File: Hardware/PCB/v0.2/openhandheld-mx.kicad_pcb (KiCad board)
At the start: 4 copper layers, 84 x 42 mm, 112 parts, among them J1 TYPE-C-31-M-12, J2 SJ-3524-SMT-TR, J3 Battery, J4 1040310811, J5 PPPC062LFBN-RC, Q1 SI2102-TP, Q2 SI2102-TP, Q3 SI2102-TP, Q4 SI2101-TP, Q5 SI2102-TP, SW1 RESET, SW2 ON/OFF, SW3 A, SW4 B, SW5 START, SW6 SELECT, U1 TLV9061IDCKR, U10 LIS2DE12TR, U11 TLV74333PDBVR, U2 CP2102N-A02-GQFN24, U3 MCP73831T-2ACI_OT, U4 PAM8301AAF, U5 DSC6001CI1A-008.0000T, U6 VSOP38338, U7 AP9211S-AN-HAC-7, U8 STM32L431CCU6, U9 W25Q64JVZPIQ

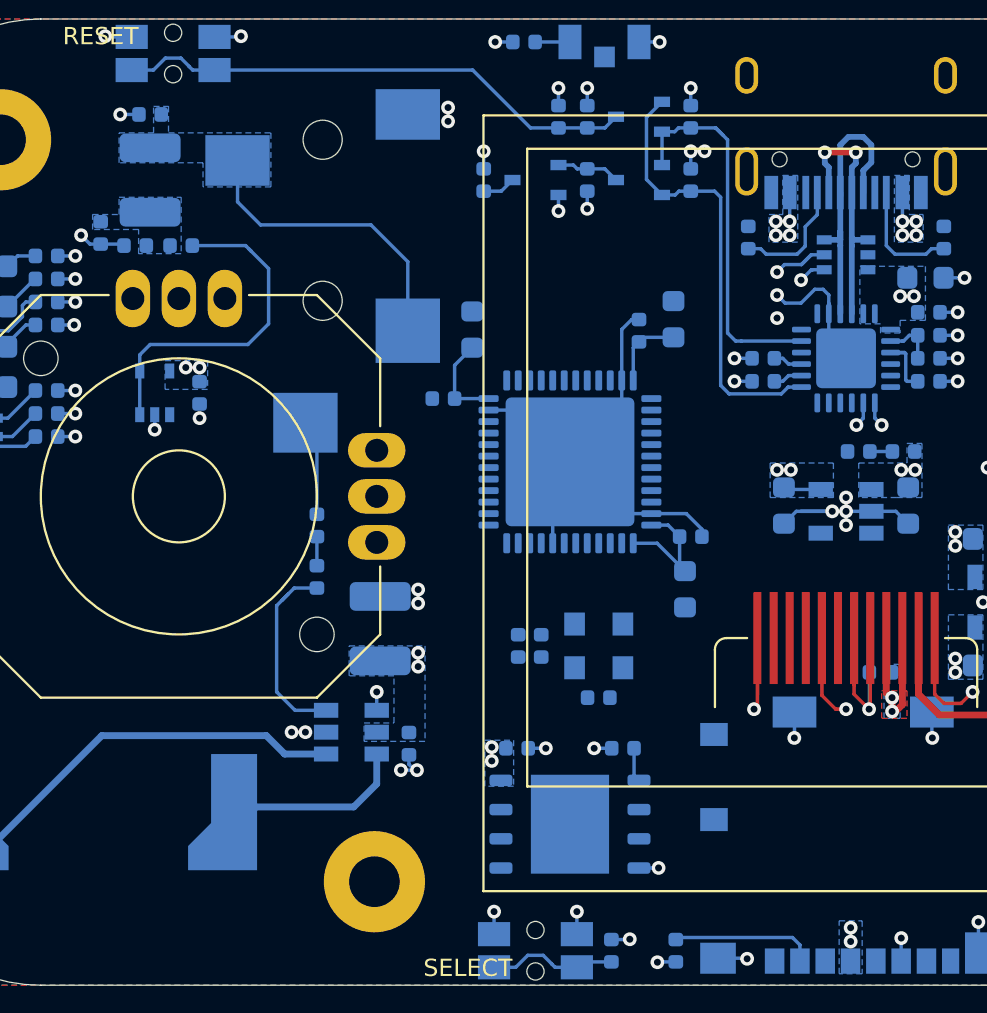
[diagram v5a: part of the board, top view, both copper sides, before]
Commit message: PCB v0.2: STM32 fanout
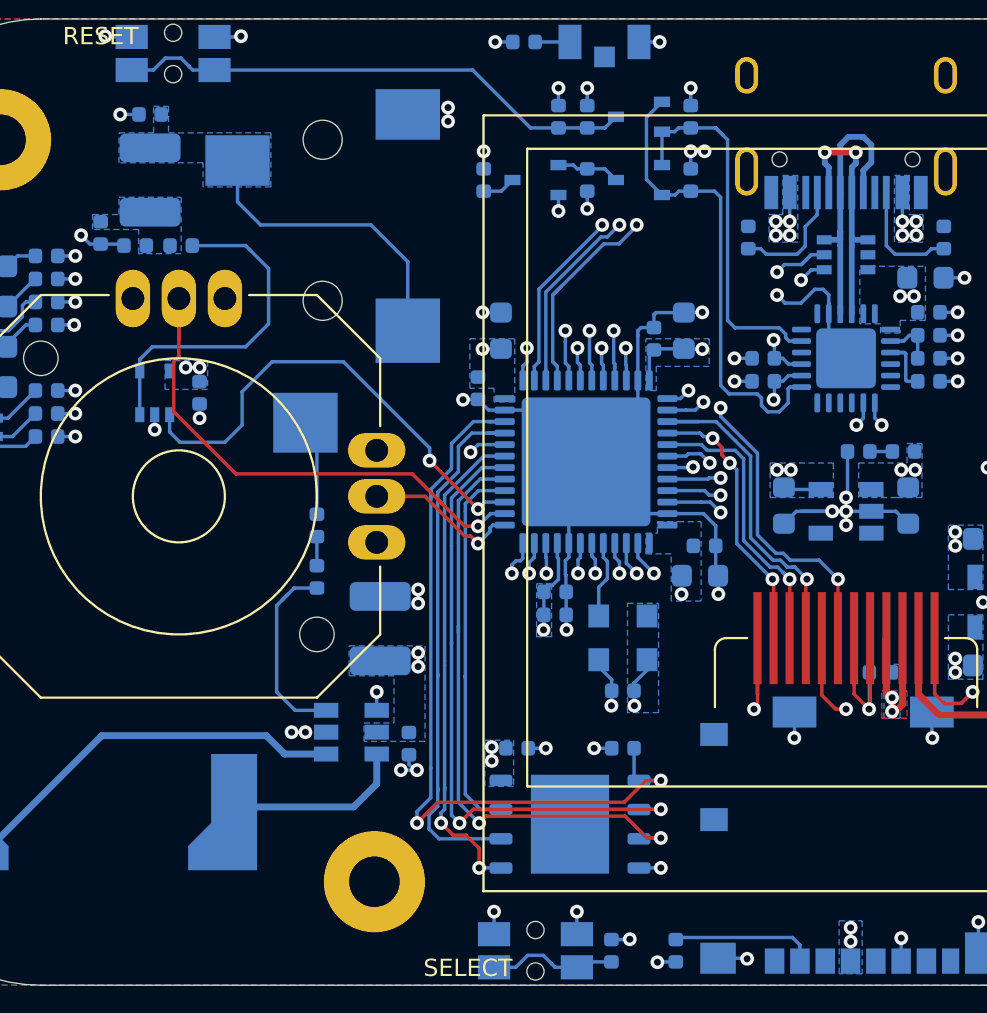
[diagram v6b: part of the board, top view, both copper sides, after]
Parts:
- moved C12 2.43 mm to (-12.7, 3.90), turned to 0 degrees
- moved C10 2.09 mm to (-12.7, 4.90), turned to 0 degrees
- moved C15 1.57 mm to (-16.0, -4.95), turned to 270 degrees
- moved C13 1.25 mm to (-15.0, -7.45)
- moved U5 1.11 mm to (-9.70, 5.90)
- moved C11 1.09 mm to (-9.70, 8.20)
- moved C20 0.88 mm to (-6.35, 3.20), turned to 0 degrees
- moved C19 0.74 mm to (-8.35, -7.10)
- moved C21 0.72 mm to (-6.15, 1.90)
- moved U8 0.70 mm to (-11.3, -1.75)
- moved C17 0.67 mm to (-7.05, -7.45)
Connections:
- D2 pad 2: /LED_RX -> /LED_RXD
- D3 pad 2: /LED_TX -> /LED_TXD
- R11 pad 2: /LED_RX -> /LED_RXD
- R13 pad 2: /LED_TX -> /LED_TXD
- U8 pad 13: /JOY_X -> /JOY_Y
- U8 pad 14: /JOY_Y -> /JOY_X
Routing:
- net /QSPI_NCS: track 1.48 -> 34.7 mm, vias 0 -> 2
- net /QSPI_IO1: track 0.00 -> 27.2 mm, vias 0 -> 2
- net /QSPI_IO2: track 0.00 -> 26.5 mm, vias 0 -> 2
- net /JOY_X: track 0.00 -> 24.2 mm, vias 0 -> 1
- net /QSPI_CLK: track 0.00 -> 23.7 mm
- net /QSPI_IO0: track 0.00 -> 21.7 mm, vias 0 -> 2
- net /DAC_PWM_OUT: track 0.00 -> 20.9 mm, vias 0 -> 2
- net /QSPI_IO3: track 0.00 -> 16.5 mm
- net GND: track 106.2 -> 122.4 mm, vias 59 -> 64
- net /LCD_DC: track 0.00 -> 15.2 mm, vias 0 -> 3
- net /LCD_SCK: track 0.00 -> 15.0 mm, vias 0 -> 1
- net /LCD_MOSI: track 0.00 -> 12.8 mm, vias 0 -> 1
- net /LCD_RESET: track 0.00 -> 11.8 mm, vias 0 -> 3
- net /SPI2_MOSI: track 0.00 -> 9.48 mm, vias 0 -> 1
- net /SPI2_MISO: track 0.00 -> 8.69 mm, vias 0 -> 1
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
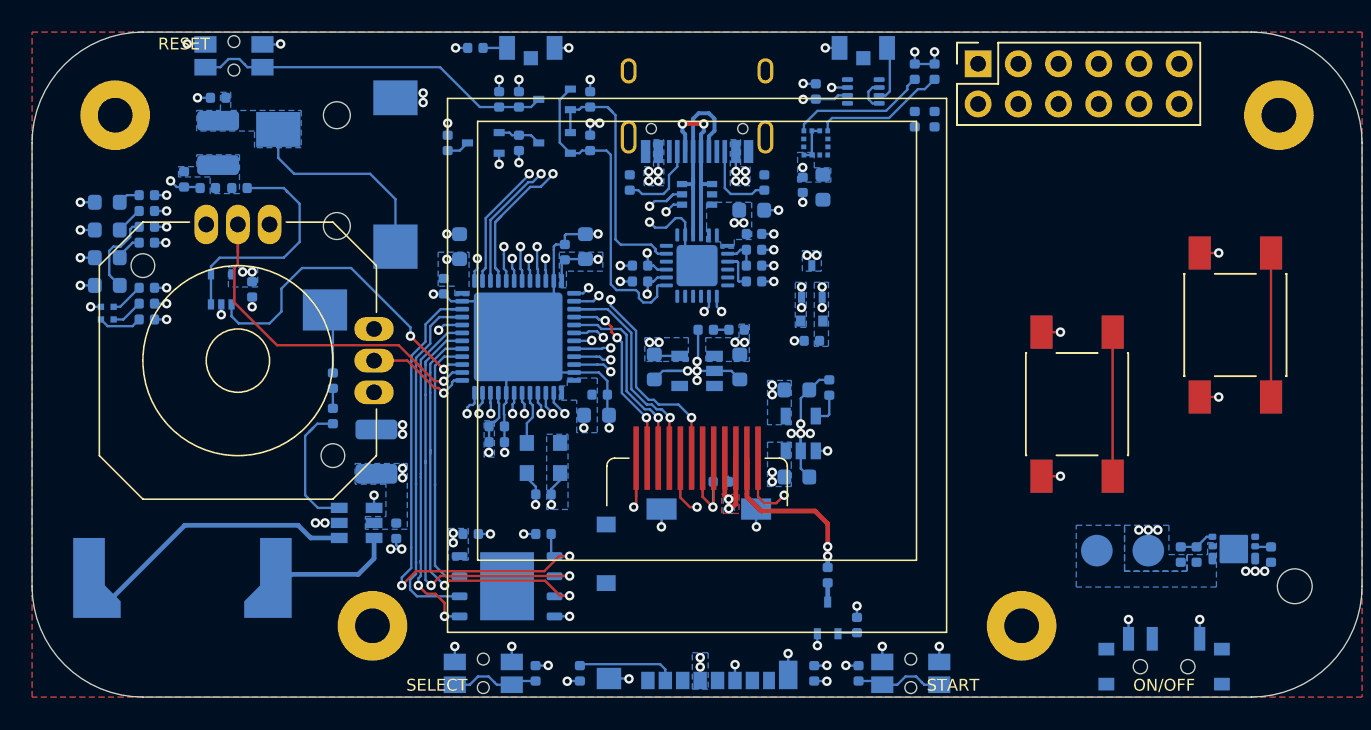
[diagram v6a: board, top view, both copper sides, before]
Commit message: PCB v0.2: Finished placement. Routing...
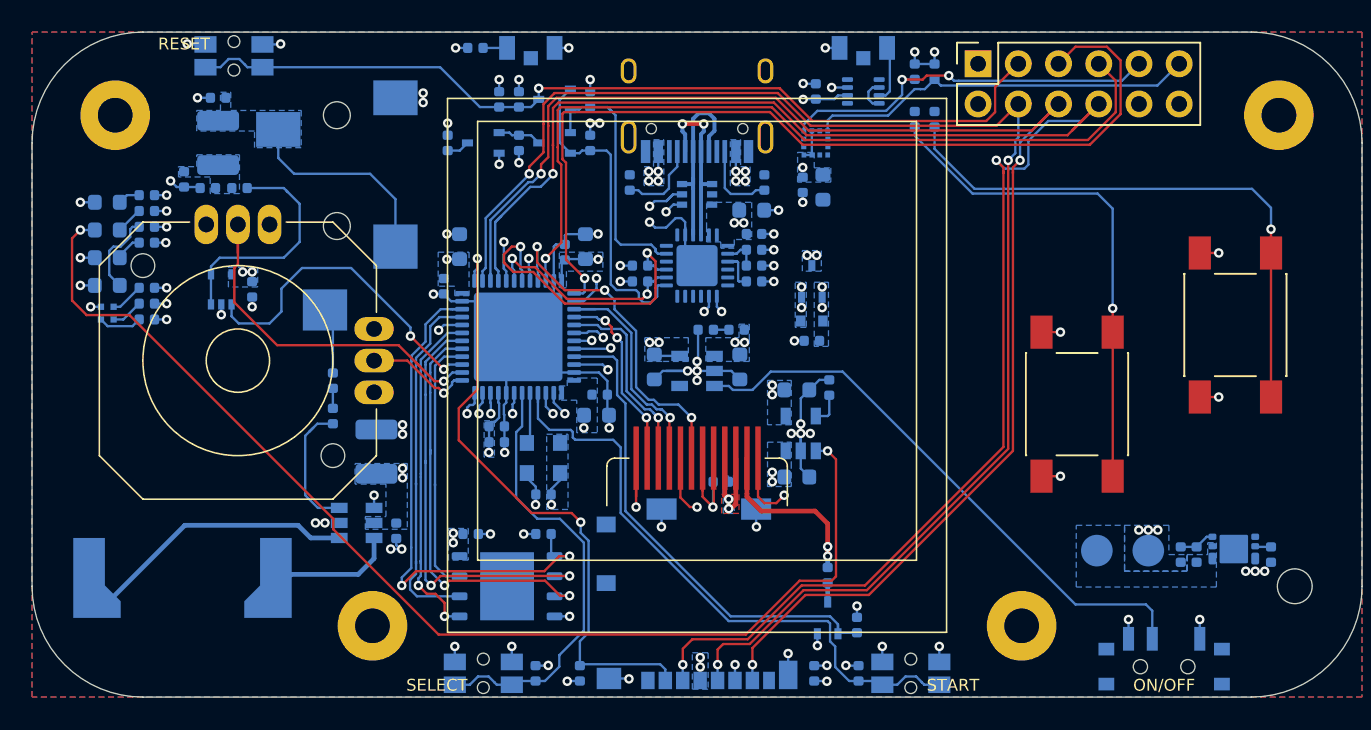
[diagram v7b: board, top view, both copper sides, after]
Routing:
- net /SPI2_MOSI: track 9.48 -> 107.6 mm, vias 1 -> 3
- net /SPI2_MISO: track 8.69 -> 96.0 mm, vias 1 -> 3
- net /SPI2_SCK: track 7.98 -> 92.1 mm, vias 1 -> 3
- net /CHG_STAT: track 1.66 -> 73.4 mm
- net /SWCLK: track 1.06 -> 57.6 mm
- net /SWDIO: track 1.42 -> 51.7 mm
- net /EN: track 0.00 -> 36.3 mm
- net /RESET: track 24.1 -> 58.4 mm, vias 1 -> 2
- net /BTN_START: track 7.33 -> 39.3 mm, vias 1 -> 0
- net /SPI2_NSS: track 7.75 -> 39.1 mm, vias 1 -> 2
- net /LCD_LED: track 3.62 -> 31.3 mm, vias 1 -> 0
- net /BTN_B: track 10.6 -> 37.6 mm, vias 1 -> 2
- net /BTN_A: track 10.7 -> 33.5 mm, vias 1 -> 2
- net /BTN_SELECT: track 7.01 -> 28.2 mm, vias 1 -> 0
- net /I2C1_SDA: track 9.53 -> 25.8 mm
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
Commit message: PCB v0.2: Finished routing.
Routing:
- net /TXT: track 2.00 -> 90.6 mm
- net /RXT: track 2.00 -> 88.8 mm
- net /USART2_TX: track 1.63 -> 64.8 mm
- net /BTN_B: track 37.6 -> 88.4 mm, vias 2 -> 3
- net /USART2_RX: track 2.39 -> 47.2 mm
- net /IR_RX: track 2.62 -> 43.3 mm, vias 2 -> 4
- net /BTN_A: track 33.5 -> 71.2 mm, vias 2 -> 3
- net /LED_G: track 2.21 -> 33.8 mm
- net /IR_TX: track 3.03 -> 32.7 mm, vias 2 -> 4
- net /LED_R: track 4.19 -> 33.5 mm
- net /I2C1_SDA: track 25.8 -> 54.9 mm, vias 1 -> 2
- net /LED_B: track 2.17 -> 28.4 mm
- net /I2C1_SCL: track 27.0 -> 52.3 mm, vias 3 -> 4
- net /RESET: track 58.4 -> 82.6 mm, vias 2 -> 3
- net /BOOT0: track 3.78 -> 26.5 mm, vias 1 -> 2
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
